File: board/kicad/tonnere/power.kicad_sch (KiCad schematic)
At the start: 42 parts, among them J12 Conn_01x05, Q2 DMN2058U, SW1 SA-0-102-C04-0004-WP, U15 TPS62903RPJR, U16 TPS62903RPJR, U22 TPS62903RPJR

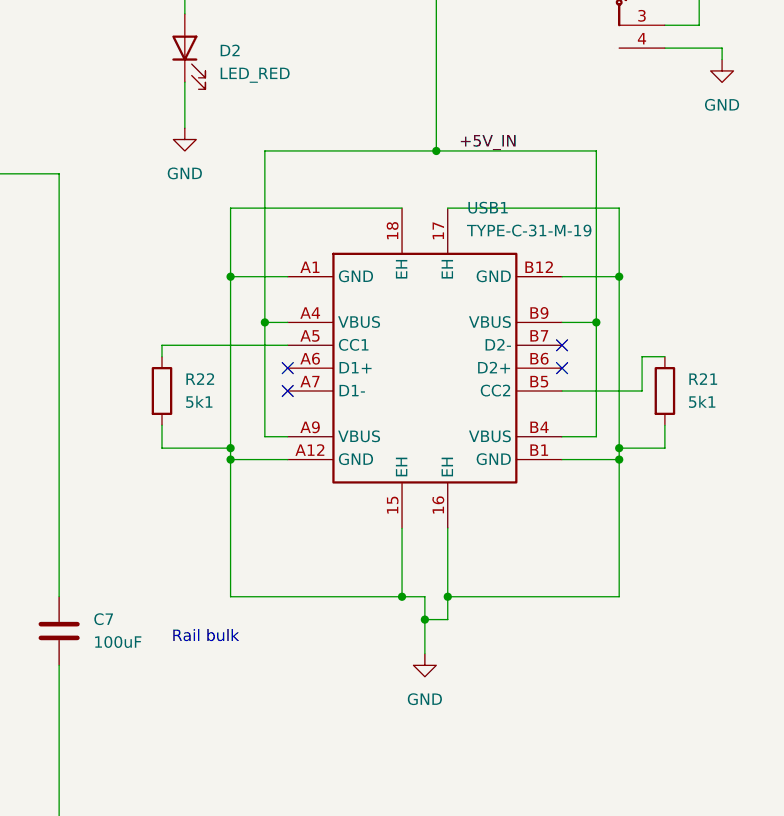
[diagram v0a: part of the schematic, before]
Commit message: Changed USB C flag connector to one with longer pins. JLCPCB did not like the existing one.
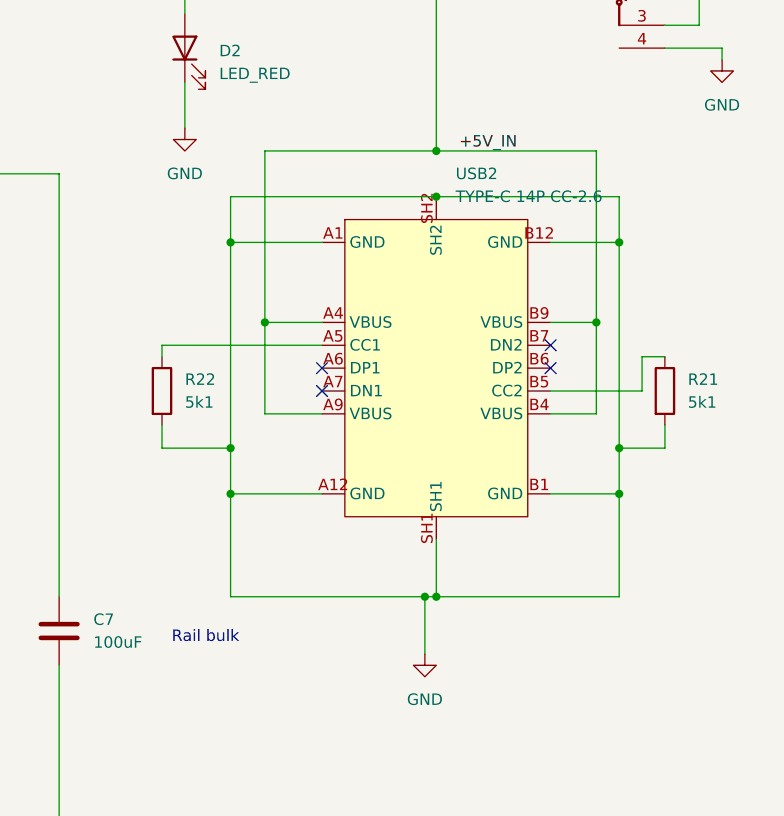
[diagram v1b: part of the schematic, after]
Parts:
- removed USB1: TYPE-C-31-M-19, usb_c_flag:USB-C-TH_TYPE-C-31-M-19, symbol usb_c_flag:TYPE-C-31-M-19
- added USB2: TYPE-C 14P CC-2.6, tonnere:TYPE-C-TH_TYPE-C-14P-CC-2.6, symbol tonnere:TYPE-C14PCC-2.6
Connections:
- net +5V_IN: now also USB2.A4 (VBUS), USB2.A9 (VBUS), USB2.B4 (VBUS), USB2.B9 (VBUS)
- net GND: now also USB2.A1 (GND), USB2.A12 (GND), USB2.B1 (GND), USB2.B12 (GND), USB2.SH1, USB2.SH2
- net at R22.1: now also USB2.A5 (CC1)
- net at R21.1: now also USB2.B5 (CC2)

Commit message: Changed video dac to 5 bit R2R and 6th-8th bits as pattern and/or sigma delta.
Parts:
- renumbered C12 to C13, C14 to C15, C19 to C20, C31 to C32, C37 to C38, C41 to C42, C42 to C43, C45 to C46, C50 to C51, C7 to C8, J12 to J11, R16 to R14, R17 to R15, R18 to R16, R19 to R17, R52 to R55, U15 to U16, U16 to U17, U22 to U23, USB2 to USB1
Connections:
- net Net-(U15-SS/TR): now reaches C13.1, U16.8 (SS/TR)
- net Net-(U22-SW): now reaches L3.2, U23.2 (SW)
- net Net-(U16-FB/VSET): now reaches R40.1, U17.9 (FB/VSET)
- net Net-(USB2-CC1): now reaches R22.1, USB1.A5 (CC1)
- net unconnected-(USB2-DP1-PadA6): now reaches USB1.A6 (DP1)
- net unconnected-(USB2-DN1-PadA7): now reaches USB1.A7 (DN1)
- net Net-(USB2-CC2): now reaches R21.1, USB1.B5 (CC2)
- net unconnected-(USB2-DP2-PadB6): now reaches USB1.B6 (DP2)
- net unconnected-(USB2-DN2-PadB7): now reaches USB1.B7 (DN2)
- net Net-(U15-MODE/S-CONF): now reaches R32.1, U16.7 (MODE/S-CONF)
- net Net-(U16-PG): now reaches R44.2, U17.1 (PG), U23.5 (EN)
- net Net-(U16-SW): now reaches L2.2, U17.2 (SW)
- net Net-(U15-PG): now reaches R45.2, U16.1 (PG), U17.5 (EN)
- net Net-(U16-MODE/S-CONF): now reaches R41.1, U17.7 (MODE/S-CONF)
- net Net-(U16-SS/TR): now reaches C32.1, U17.8 (SS/TR)
- net unconnected-(U22-PG-Pad1): now reaches U23.1 (PG)
- net Net-(U22-MODE/S-CONF): now reaches R55.1, U23.7 (MODE/S-CONF)
- net Net-(U22-SS/TR): now reaches C43.1, U23.8 (SS/TR)
- net unconnected-(U22-FB/VSET-Pad9): now reaches U23.9 (FB/VSET)
- net Net-(U15-SW): now reaches L1.2, U16.2 (SW)
